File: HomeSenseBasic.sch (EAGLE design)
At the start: 21 parts, among them IC1 ESP12SMT, IC3 MS563702BA03, IC4 DHT12

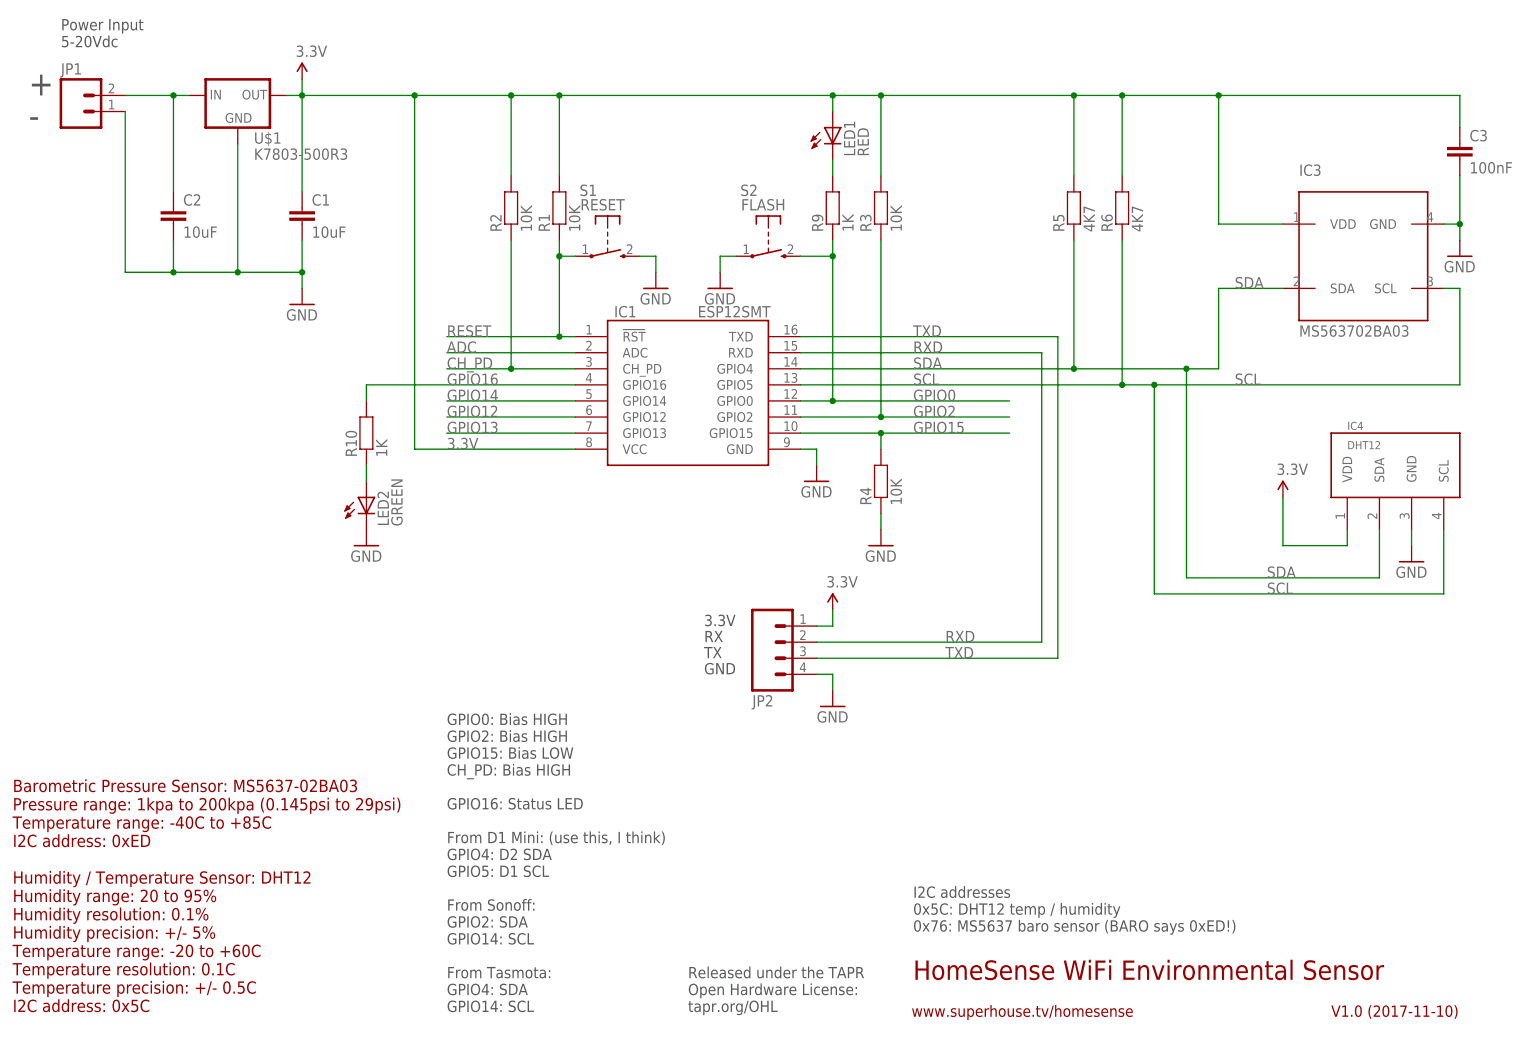
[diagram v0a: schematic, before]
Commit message: Updated routing and schematic for v1.0 release
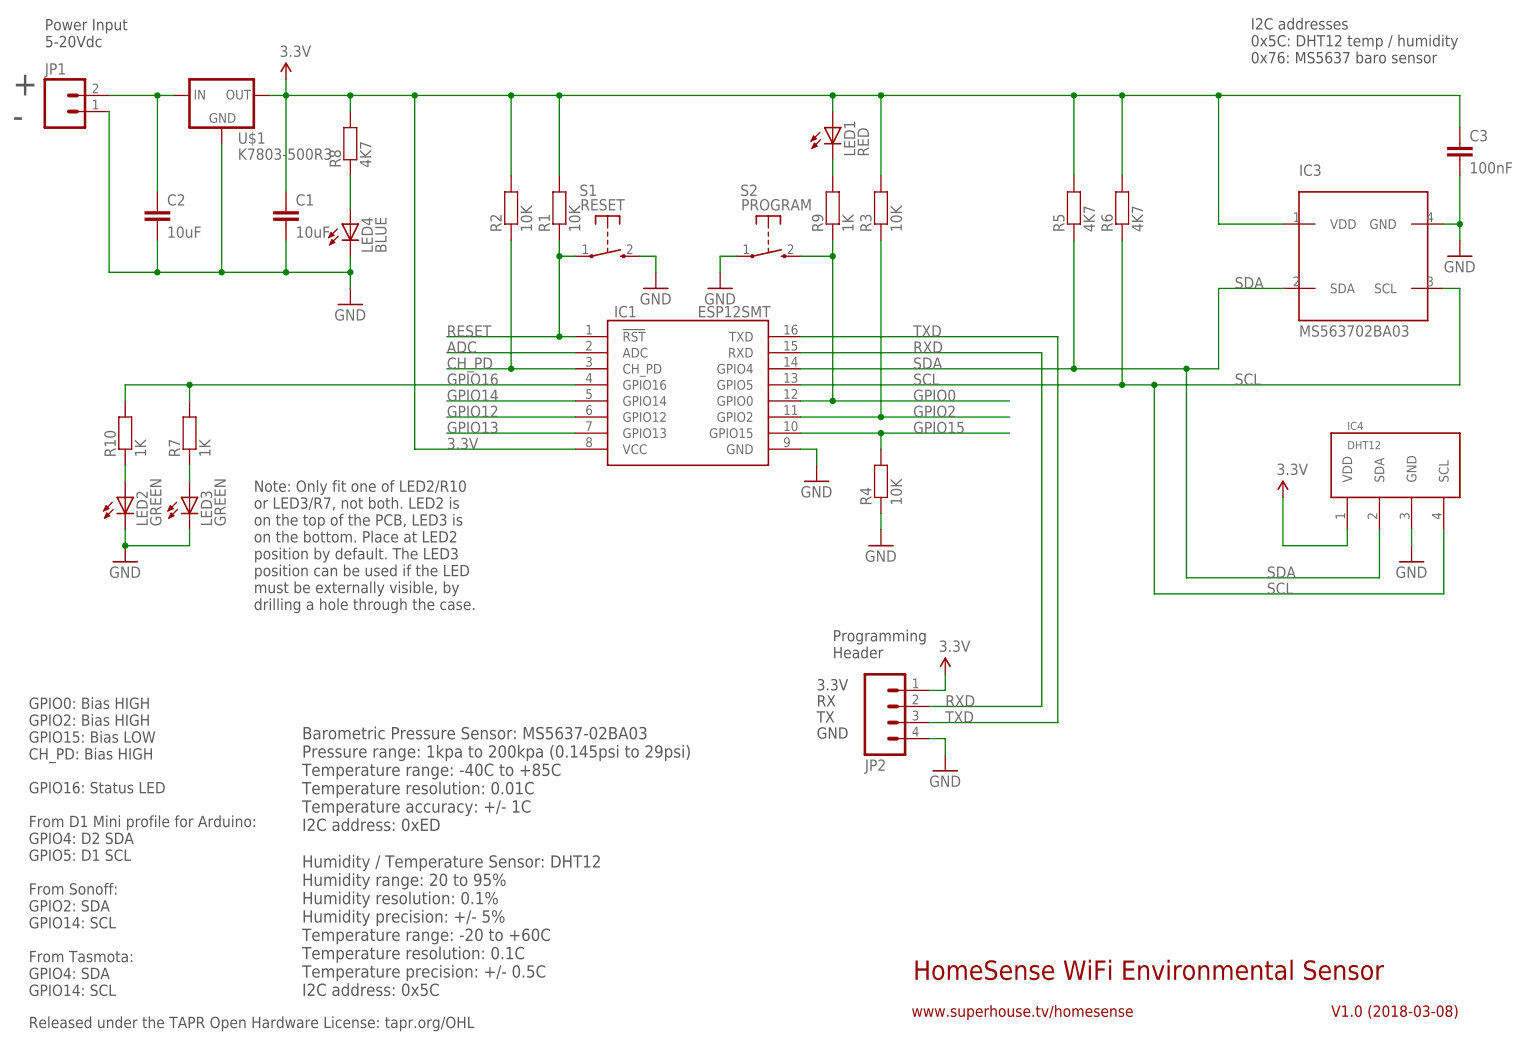
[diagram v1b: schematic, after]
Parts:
- added LED3: GREEN, freetronics-jon:LED0603
- added LED4: BLUE, freetronics-jon:LED0603
- added R7: 1K, freetronics-jon:RESISTOR0603
- added R8: 4K7, freetronics-jon:RESISTOR0603
- S2: value FLASH -> PROGRAM
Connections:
- new net N$11: LED3.A, R7.1
- new net N$2: LED4.A, R8.1
- net 3.3V: now also R8.2
- net GND: now also LED3.C, LED4.C
- net GPIO16: now also R7.2
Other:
- note added: "Barometric Pressure Sensor: MS5637-02BA03 Pressure range: 1kpa to 200kpa (0.145psi to 29psi) Temperature range: -40C to +85C Temperature resolution: 0.01C Temperature accuracy: +/- 1C I2C address: 0xED Humidity / Temperature Sensor: DHT12 Humidity range: 20 to 95% Humidity resolution: 0.1% Humidity precision: +/- 5% Temperature range: -20 to +60C Temperature resolution: 0.1C Temperature precision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"
- note added: "GPIO0: Bias HIGH GPIO2: Bias HIGH GPIO15: Bias LOW CH_PD: Bias HIGH GPIO16: Status LED From D1 Mini profile for Arduino: GPIO4: D2 SDA GPIO5: D1 SCL From Sonoff: GPIO2: SDA GPIO14: SCL From Tasmota: GPIO4: SDA GPIO14: SCL"
- note added: "I2C addresses 0x5C: DHT12 temp / humidity 0x76: MS5637 baro sensor"
- note added: "Note: Only fit one of LED2/R10 or LED3/R7, not both. LED2 is on the top of the PCB, LED3 is on the bottom. Place at LED2 position by default. The LED3 position can be used if the LED must be externally visible, by drilling a hole through the case."
- note added: "Programming Header"
- note added: "V1.0 (2018-03-08)"
- note removed: "Barometric Pressure Sensor: MS5637-02BA03 Pressure range: 1kpa to 200kpa (0.145psi to 29psi) Temperature range: -40C to +85C I2C address: 0xED Humidity / Temperature Sensor: DHT12 Humidity range: 20 to 95% Humidity resolution: 0.1% Humidity precision: +/- 5% Temperature range: -20 to +60C Temperature resolution: 0.1C Temperature precision: +/- 0.5C I2C address: 0x5C"
- note removed: "GPIO0: Bias HIGH GPIO2: Bias HIGH GPIO15: Bias LOW CH_PD: Bias HIGH GPIO16: Status LED From D1 Mini: (use this, I think) GPIO4: D2 SDA GPIO5: D1 SCL From Sonoff: GPIO2: SDA GPIO14: SCL From Tasmota: GPIO4: SDA GPIO14: SCL"
- note removed: "I2C addresses 0x5C: DHT12 temp / humidity 0x76: MS5637 baro sensor (BARO says 0xED!)"
- note removed: "V1.0 (2017-11-10)"
- moved on the sheet: C1, C2, JP1, JP2, LED2, R10, U$1

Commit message: Fixed ESP12 footprint with correct GPIO4/5
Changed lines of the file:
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@@
 <?xml version="1.0" encoding="utf-8"?>
 <!DOCTYPE eagle SYSTEM "eagle.dtd">
-<eagle version="8.6.0">
+<eagle version="8.7.0">
 <drawing>
 <settings>
@@
 <setting verticaltext="up"/>
 </settings>
-<grid distance="0.1" unitdist="inch" unit="inch" style="dots" multiple="1" display="no" altdistance="0.01" altunitdist="inch" altunit="mil"/>
+<grid distance="0.1" unitdist="inch" unit="inch" style="lines" multiple="1" display="no" altdistance="0.01" altunitdist="inch" altunit="inch"/>
 <layers>
 <layer number="1" name="Top" color="4" fill="1" visible="no" active="no"/>
@@
 <net name="SDA" class="0">
 <segment>
-<pinref part="IC1" gate="G$1" pin="GPIO4"/>
-<label x="149.86" y="109.22" size="1.778" layer="95"/>
-<wire x1="132.08" y1="109.22" x2="175.26" y2="109.22" width="0.1524" layer="91"/>
+<label x="149.86" y="106.68" size="1.778" layer="95"/>
 <pinref part="R5" gate="G$1" pin="1"/>
-<wire x1="175.26" y1="109.22" x2="193.04" y2="109.22" width="0.1524" layer="91"/>
-<wire x1="193.04" y1="109.22" x2="198.12" y2="109.22" width="0.1524" layer="91"/>
-<wire x1="175.26" y1="129.54" x2="175.26" y2="109.22" width="0.1524" layer="91"/>
-<junction x="175.26" y="109.22"/>
-<wire x1="198.12" y1="109.22" x2="198.12" y2="121.92" width="0.1524" layer="91"/>
+<wire x1="175.26" y1="106.68" x2="193.04" y2="106.68" width="0.1524" layer="91"/>
+<wire x1="193.04" y1="106.68" x2="198.12" y2="106.68" width="0.1524" layer="91"/>
+<wire x1="175.26" y1="129.54" x2="175.26" y2="106.68" width="0.1524" layer="91"/>
+<wire x1="198.12" y1="106.68" x2="198.12" y2="121.92" width="0.1524" layer="91"/>
 <pinref part="IC3" gate="G$1" pin="SDA"/>
 <wire x1="198.12" y1="121.92" x2="208.28" y2="121.92" width="0.1524" layer="91"/>
@@
 <wire x1="223.52" y1="83.82" x2="223.52" y2="76.2" width="0.1524" layer="91"/>
 <wire x1="223.52" y1="76.2" x2="193.04" y2="76.2" width="0.1524" layer="91"/>
-<wire x1="193.04" y1="76.2" x2="193.04" y2="109.22" width="0.1524" layer="91"/>
-<junction x="193.04" y="109.22"/>
+<wire x1="193.04" y1="76.2" x2="193.04" y2="106.68" width="0.1524" layer="91"/>
+<junction x="193.04" y="106.68"/>
 <label x="200.66" y="121.92" size="1.778" layer="95"/>
 <label x="205.74" y="76.2" size="1.778" layer="95"/>
+<junction x="175.26" y="106.68"/>
+<pinref part="IC1" gate="G$1" pin="GPIO4"/>
+<wire x1="175.26" y1="106.68" x2="132.08" y2="106.68" width="0.1524" layer="91"/>
 </segment>
 </net>
 <net name="SCL" class="0">
 <segment>
-<pinref part="IC1" gate="G$1" pin="GPIO5"/>
-<label x="149.86" y="106.68" size="1.778" layer="95"/>
-<wire x1="132.08" y1="106.68" x2="182.88" y2="106.68" width="0.1524" layer="91"/>
+<label x="149.86" y="109.22" size="1.778" layer="95"/>
 <pinref part="R6" gate="G$1" pin="1"/>
-<wire x1="182.88" y1="129.54" x2="182.88" y2="106.68" width="0.1524" layer="91"/>
-<junction x="182.88" y="106.68"/>
+<wire x1="182.88" y1="129.54" x2="182.88" y2="109.22" width="0.1524" layer="91"/>
 <pinref part="IC3" gate="G$1" pin="SCL"/>
 <wire x1="233.68" y1="121.92" x2="236.22" y2="121.92" width="0.1524" layer="91"/>
-<wire x1="236.22" y1="121.92" x2="236.22" y2="106.68" width="0.1524" layer="91"/>
-<wire x1="236.22" y1="106.68" x2="187.96" y2="106.68" width="0.1524" layer="91"/>
+<wire x1="236.22" y1="121.92" x2="236.22" y2="109.22" width="0.1524" layer="91"/>
+<wire x1="236.22" y1="109.22" x2="187.96" y2="109.22" width="0.1524" layer="91"/>
 <pinref part="IC4" gate="G$1" pin="SCL"/>
-<wire x1="187.96" y1="106.68" x2="182.88" y2="106.68" width="0.1524" layer="91"/>
+<wire x1="187.96" y1="109.22" x2="182.88" y2="109.22" width="0.1524" layer="91"/>
 <wire x1="233.68" y1="83.82" x2="233.68" y2="73.66" width="0.1524" layer="91"/>
 <wire x1="233.68" y1="73.66" x2="187.96" y2="73.66" width="0.1524" layer="91"/>
-<wire x1="187.96" y1="73.66" x2="187.96" y2="106.68" width="0.1524" layer="91"/>
-<junction x="187.96" y="106.68"/>
-<label x="200.66" y="106.68" size="1.778" layer="95"/>
+<wire x1="187.96" y1="73.66" x2="187.96" y2="109.22" width="0.1524" layer="91"/>
+<junction x="187.96" y="109.22"/>
+<label x="200.66" y="109.22" size="1.778" layer="95"/>
 <label x="205.74" y="73.66" size="1.778" layer="95"/>
-</segment>
-</net>
+<junction x="182.88" y="109.22"/>
+<pinref part="IC1" gate="G$1" pin="GPIO5"/>
+<wire x1="182.88" y1="109.22" x2="132.08" y2="109.22" width="0.1524" layer="91"/>
+</segment>
+</net>
